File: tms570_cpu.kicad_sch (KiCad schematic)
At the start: 51 parts, among them J12 TS-103-G-A, J2 FTSH-105-01-L-DV-K, U2 TMS570LS0914PGE

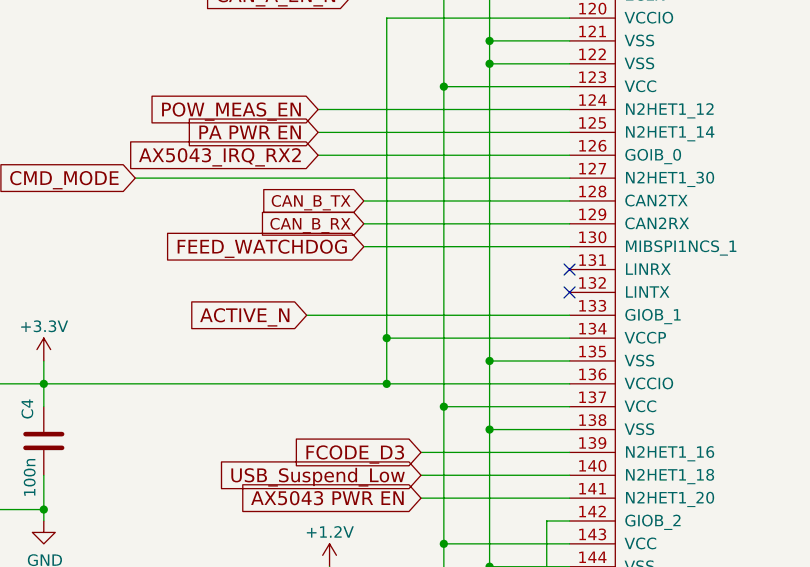
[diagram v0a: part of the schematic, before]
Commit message: Make a little more space around the MRAM
Change the orientation of some resistors.

Signed-off-by: Corey Minyard <corey@minyard.net>
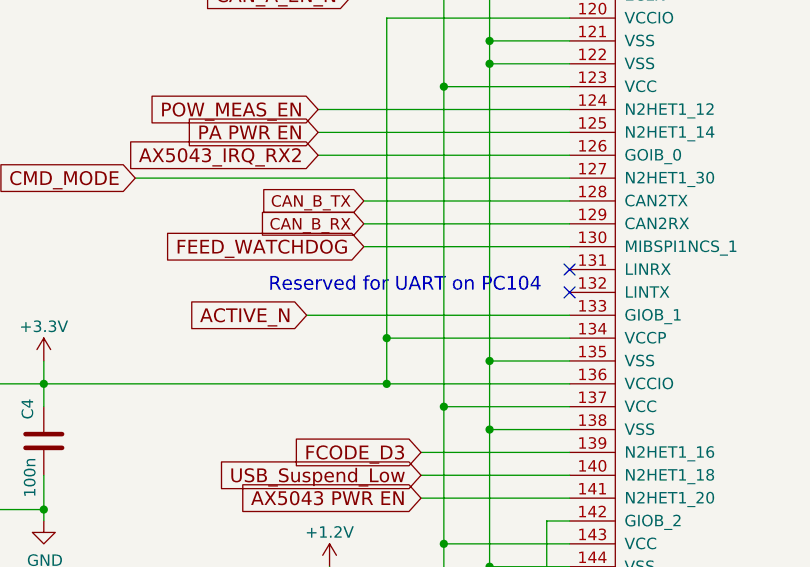
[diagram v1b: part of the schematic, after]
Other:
- note added: "Reserved for UART on PC104"
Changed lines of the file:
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@@
+		)
+	)
+	(text "Reserved for UART on PC104"
+		(exclude_from_sim no)
+		(at 131.572 154.178 0)
+		(effects
+			(font
+				(size 1.524 1.524)
+			)
 		)
 	)

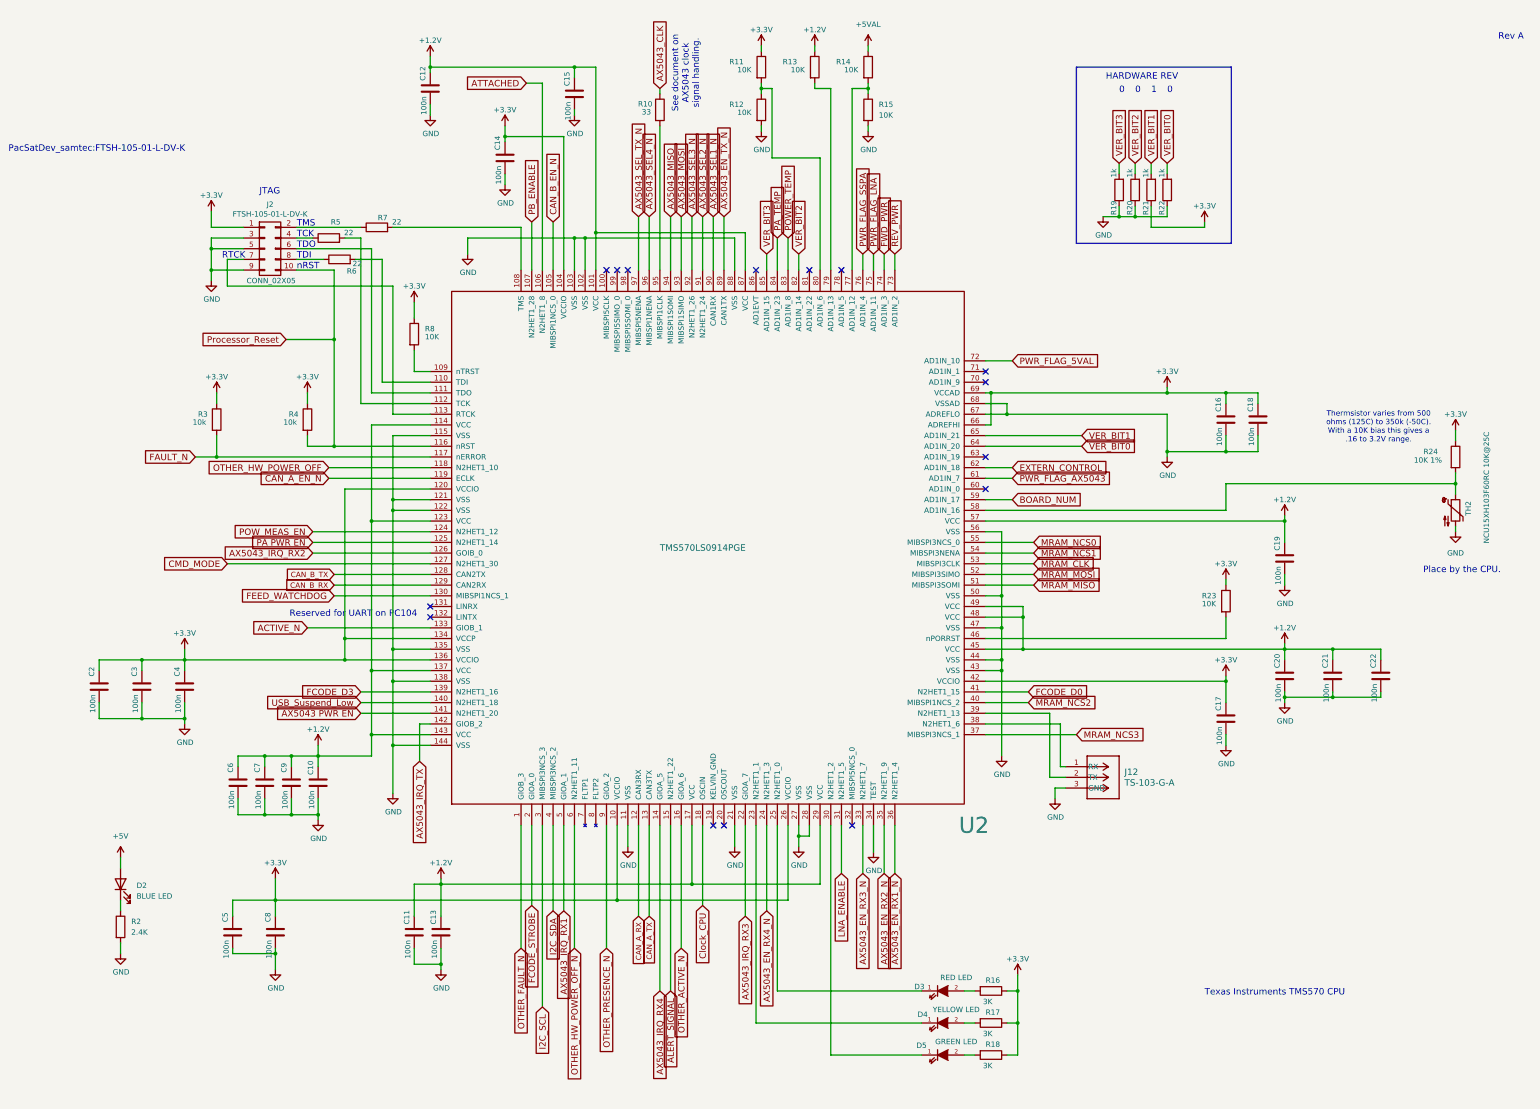
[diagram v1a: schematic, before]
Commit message: Lots of updates to ease manufacturing
Component changes, changes in the formatting of the values, etc.

Signed-off-by: Corey Minyard <corey@minyard.net>
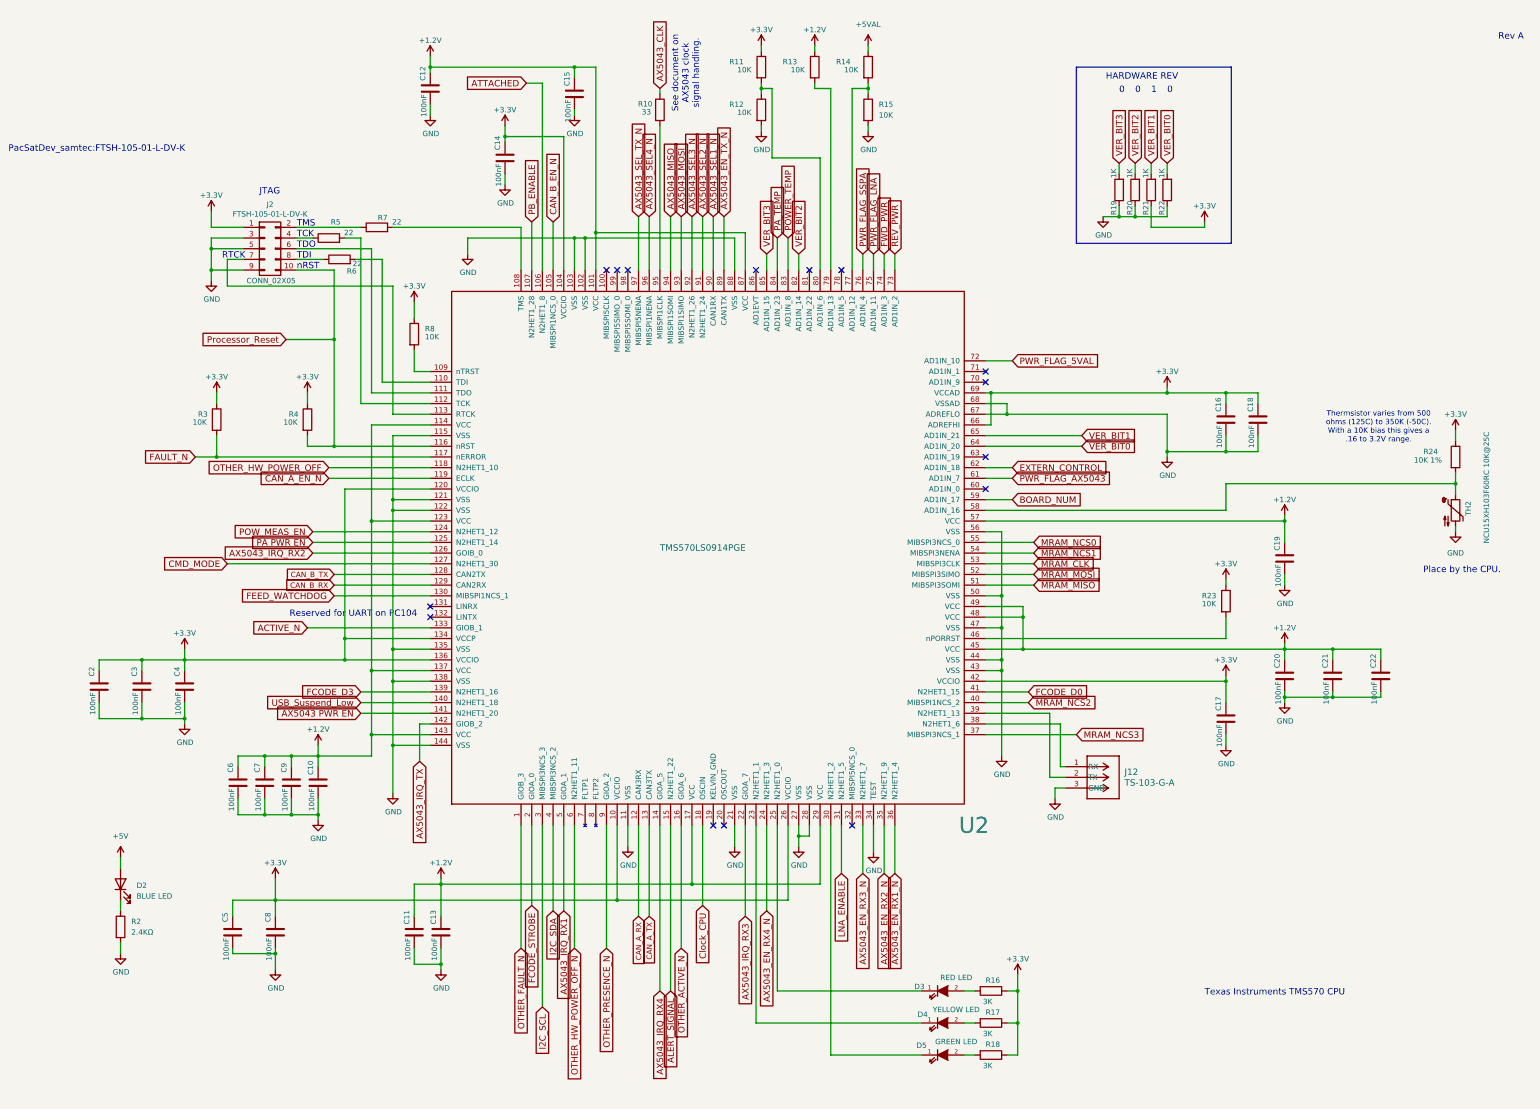
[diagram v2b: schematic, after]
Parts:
- C10, C11, C12, C13, C14, C15, C16, C17, C18, C19, C2, C20, C21, C22, C3, C4, C5, C6, C7, C8, C9: value 100n -> 100nF
- R19, R20, R21, R22: value 1k -> 1K
- R2: value 2.4K -> 2.4KΩ
- R3, R4: value 10k -> 10K
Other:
- note added: "Thermsistor varies from 500 ohms (125C) to 350K (-50C). With a 10K bias this gives a .16 to 3.2V range."
- note removed: "Thermsistor varies from 500 ohms (125C) to 350k (-50C). With a 10K bias this gives a .16 to 3.2V range."
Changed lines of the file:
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@@
 		)
 	)
-	(text "Thermsistor varies from 500\nohms (125C) to 350k (-50C).\nWith a 10K bias this gives a\n.16 to 3.2V range."
+	(text "Thermsistor varies from 500\nohms (125C) to 350K (-50C).\nWith a 10K bias this gives a\n.16 to 3.2V range."
 		(exclude_from_sim no)
 		(at 375.412 109.728 0)
@@
 			)
 		)
-		(property "Value" "10k"
+		(property "Value" "10K"
 			(at 114.935 108.585 0)
 			(effects
@@
 			)
 		)
-		(property "Value" "10k"
+		(property "Value" "10K"
 			(at 93.345 108.585 0)
 			(effects
@@
 			)
 		)
-		(property "Value" "1k"
+		(property "Value" "1K"
 			(at 312.42 48.26 90)
 			(effects
@@
 			)
 		)
-		(property "Value" "1k"
+		(property "Value" "1K"
 			(at 316.23 48.26 90)
 			(effects
@@
 			)
 		)
-		(property "Value" "1k"
+		(property "Value" "1K"
 			(at 320.04 48.26 90)
 			(effects
@@
 			)
 		)
-		(property "Value" "1k"
+		(property "Value" "1K"
 			(at 323.85 48.26 90)
 			(effects
@@
 			)
 		)
-		(property "Value" "100n"
+		(property "Value" "100nF"
 			(at 111.506 233.934 90)
 			(effects
@@
 			)
 		)
-		(property "Value" "100n"
+		(property "Value" "100nF"
 			(at 121.666 198.374 90)
 			(effects
@@
 			)
 		)
-		(property "Value" "100n"
+		(property "Value" "100nF"
 			(at 351.536 145.034 90)
 			(effects
@@
 			)
 		)
-		(property "Value" "100n"
+		(property "Value" "100nF"
 			(at 150.876 233.934 90)
 			(effects
@@
 			)
 		)
-		(property "Value" "100n"
+		(property "Value" "100nF"
 			(at 108.966 198.374 90)
 			(effects
@@
 			)
 		)
-		(property "Value" "100n"
+		(property "Value" "100nF"
 			(at 345.186 112.014 90)
 			(effects
@@
 			)
 		)
-		(property "Value" "100n"
+		(property "Value" "100nF"
 			(at 351.536 172.974 90)
 			(effects
@@
 			)
 		)
-		(property "Value" "100n"
+		(property "Value" "100nF"
 			(at 79.756 175.514 90)
 			(effects
@@
 			)
 		)
-		(property "Value" "100n"
+		(property "Value" "100nF"
 			(at 101.346 233.934 90)
 			(effects
@@
 			)
 		)
-		(property "Value" "100n"
+		(property "Value" "100nF"
 			(at 115.316 198.374 90)
 			(effects
@@
 		(fields_autoplaced yes)
 		(property "Reference" "R2"
-			(at 78.74 227.33 0)
+			(at 78.74 227.3299 0)
 			(effects
 				(font
@@
 			)
 		)
-		(property "Value" "2.4K"
-			(at 78.74 229.87 0)
+		(property "Value" "2.4KΩ"
+			(at 78.74 229.8699 0)
 			(effects
 				(font
@@
 			)
 		)
-		(property "Value" "100n"
+		(property "Value" "100nF"
 			(at 166.116 49.784 90)
 			(effects
@@
 			)
 		)
-		(property "Value" "100n"
+		(property "Value" "100nF"
 			(at 148.336 33.274 90)
 			(effects
@@
 			)
 		)
-		(property "Value" "100n"
+		(property "Value" "100nF"
 			(at 362.966 172.974 90)
 			(effects
@@
 			)
 		)
-		(property "Value" "100n"
+		(property "Value" "100nF"
 			(at 182.626 34.544 90)
 			(effects
@@
 			)
 		)
-		(property "Value" "100n"
+		(property "Value" "100nF"
 			(at 89.916 175.514 90)
 			(effects
@@
 			)
 		)
-		(property "Value" "100n"
+		(property "Value" "100nF"
 			(at 337.566 112.014 90)
 			(effects
@@
 			)
 		)
-		(property "Value" "100n"
+		(property "Value" "100nF"
 			(at 144.526 233.934 90)
 			(effects
@@
 			)
 		)
-		(property "Value" "100n"
+		(property "Value" "100nF"
 			(at 69.596 175.514 90)
 			(effects
@@
 			)
 		)
-		(property "Value" "100n"
+		(property "Value" "100nF"
 			(at 374.396 172.974 90)
 			(effects
@@
 			)
 		)
-		(property "Value" "100n"
+		(property "Value" "100nF"
 			(at 337.566 183.134 90)
 			(effects
@@
 			)
 		)
-		(property "Value" "100n"
+		(property "Value" "100nF"
 			(at 102.616 198.374 90)
 			(effects

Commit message: Update all resistors to have an ohm symbol
Make it more clean in the BOM what they are.

Signed-off-by: Corey Minyard <corey@minyard.net>
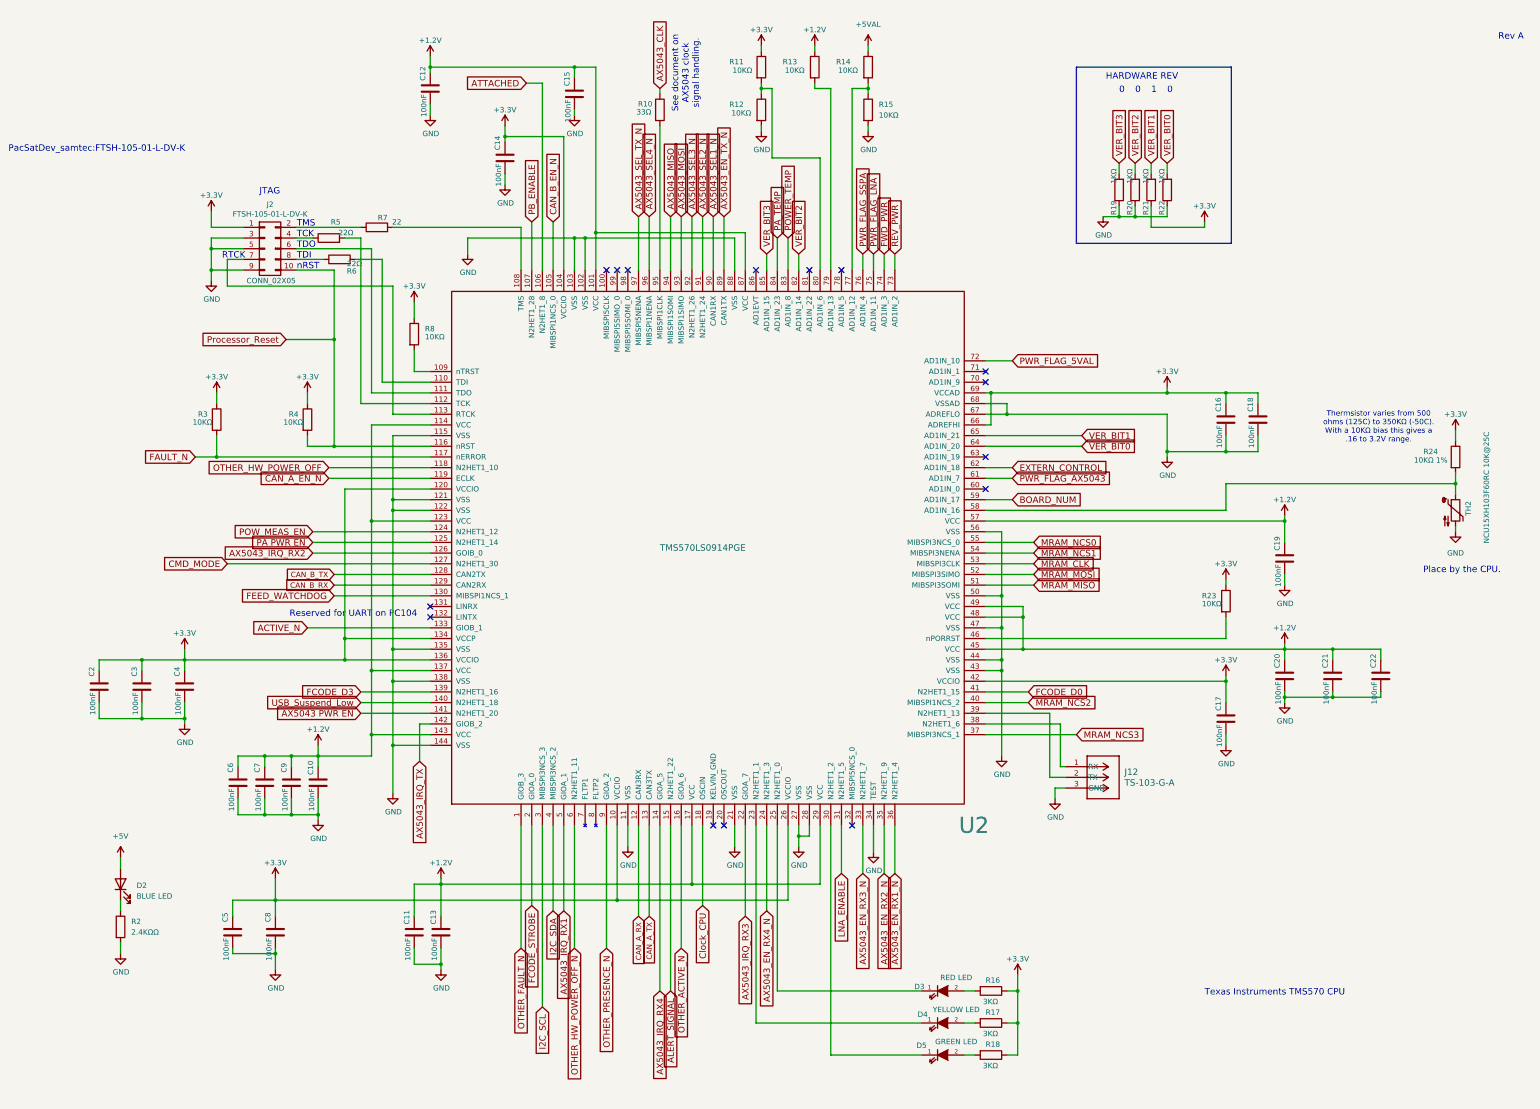
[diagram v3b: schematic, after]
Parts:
- R10: value 33 -> 33Ω
- R11, R12, R13, R14, R15, R23, R3, R4, R8: value 10K -> 10KΩ
- R16, R17, R18: value 3K -> 3KΩ
- R19, R20, R21, R22: value 1K -> 1KΩ
- R2: value 2.4KΩ -> 2.4KΩΩ
- R24: value 10K 1% -> 10KΩ 1%
- R5, R6: value 22 -> 22Ω
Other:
- note added: "Thermsistor varies from 500 ohms (125C) to 350KΩ (-50C). With a 10KΩ bias this gives a .16 to 3.2V range."
- note removed: "Thermsistor varies from 500 ohms (125C) to 350K (-50C). With a 10K bias this gives a .16 to 3.2V range."
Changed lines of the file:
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@@
 		)
 	)
-	(text "Thermsistor varies from 500\nohms (125C) to 350K (-50C).\nWith a 10K bias this gives a\n.16 to 3.2V range."
+	(text "Thermsistor varies from 500\nohms (125C) to 350KΩ (-50C).\nWith a 10KΩ bias this gives a\n.16 to 3.2V range."
 		(exclude_from_sim no)
 		(at 375.412 109.728 0)
@@
 			)
 		)
-		(property "Value" "10K"
+		(property "Value" "10KΩ"
 			(at 114.935 108.585 0)
 			(effects
@@
 			)
 		)
-		(property "Value" "10K"
+		(property "Value" "10KΩ"
 			(at 148.59 88.265 0)
 			(effects
@@
 			)
 		)
-		(property "Value" "10K"
+		(property "Value" "10KΩ"
 			(at 93.345 108.585 0)
 			(effects
@@
 			)
 		)
-		(property "Value" "3K"
+		(property "Value" "3KΩ"
 			(at 281.305 246.38 90)
 			(effects
@@
 			)
 		)
-		(property "Value" "3K"
+		(property "Value" "3KΩ"
 			(at 281.305 254 90)
 			(effects
@@
 			)
 		)
-		(property "Value" "3K"
+		(property "Value" "3KΩ"
 			(at 281.305 261.62 90)
 			(effects
@@
 			)
 		)
-		(property "Value" "10K"
+		(property "Value" "10KΩ"
 			(at 333.375 151.765 0)
 			(effects
@@
 			)
 		)
-		(property "Value" "1K"
+		(property "Value" "1KΩ"
 			(at 312.42 48.26 90)
 			(effects
@@
 			)
 		)
-		(property "Value" "1K"
+		(property "Value" "1KΩ"
 			(at 316.23 48.26 90)
 			(effects
@@
 			)
 		)
-		(property "Value" "1K"
+		(property "Value" "1KΩ"
 			(at 320.04 48.26 90)
 			(effects
@@
 			)
 		)
-		(property "Value" "1K"
+		(property "Value" "1KΩ"
 			(at 323.85 48.26 90)
 			(effects
@@
 			)
 		)
-		(property "Value" "10K"
-			(at 235.585 24.765 0)
+		(property "Value" "10KΩ"
+			(at 234.188 24.892 0)
 			(effects
 				(font
@@
 			)
 		)
-		(property "Value" "10K"
-			(at 248.285 24.765 0)
+		(property "Value" "10KΩ"
+			(at 246.888 24.892 0)
 			(effects
 				(font
@@
 			)
 		)
-		(property "Value" "10K"
+		(property "Value" "10KΩ"
 			(at 256.54 35.56 0)
 			(effects
@@
 			)
 		)
-		(property "Value" "10K 1%"
+		(property "Value" "10KΩ 1%"
 			(at 383.794 117.602 0)
 			(effects
@@
 			)
 		)
-		(property "Value" "10K"
-			(at 222.885 34.925 0)
+		(property "Value" "10KΩ"
+			(at 221.488 35.052 0)
 			(effects
 				(font
@@
 			)
 		)
-		(property "Value" "22"
+		(property "Value" "22Ω"
 			(at 131.572 63.5 90)
 			(effects
@@
 			)
 		)
-		(property "Value" "2.4KΩ"
+		(property "Value" "2.4KΩΩ"
 			(at 78.74 229.8699 0)
 			(effects
@@
 			)
 		)
-		(property "Value" "10K"
-			(at 222.885 24.765 0)
+		(property "Value" "10KΩ"
+			(at 221.742 24.892 0)
 			(effects
 				(font
@@
 			)
 		)
-		(property "Value" "22"
+		(property "Value" "22Ω"
 			(at 133.604 70.866 90)
 			(effects
@@
 			)
 		)
-		(property "Value" "33"
-			(at 200.152 34.798 0)
+		(property "Value" "33Ω"
+			(at 198.882 34.798 0)
 			(effects
 				(font

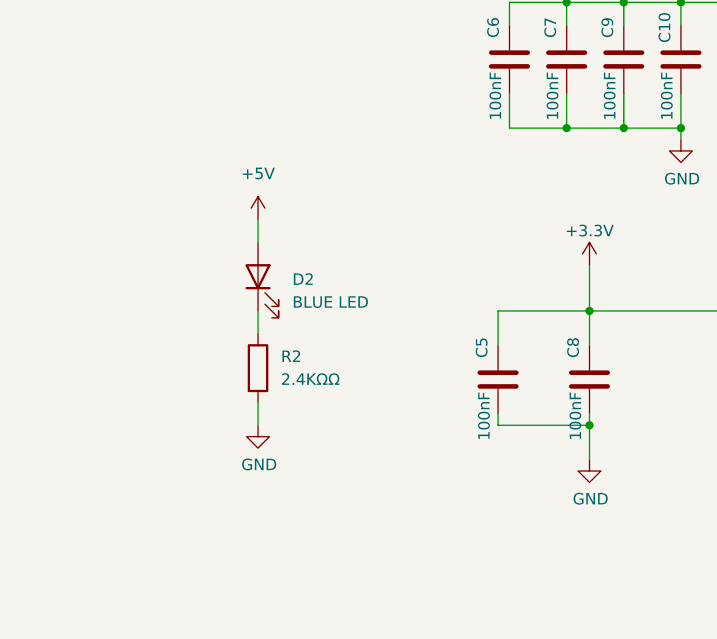
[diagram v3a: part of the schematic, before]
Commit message: More work converting to the CubeSat Kit Bus
Signed-off-by: Corey Minyard <corey@minyard.net>
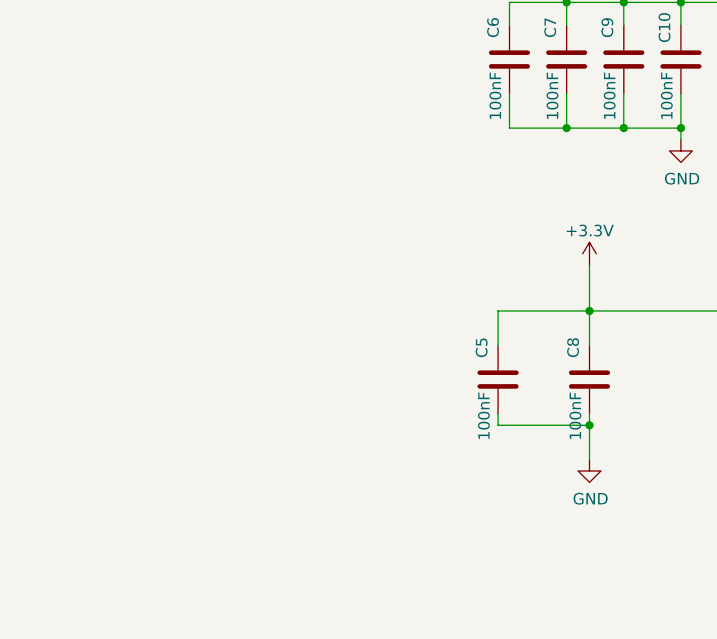
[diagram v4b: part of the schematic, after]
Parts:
- removed D2: BLUE LED, LED_SMD:LED_0603_1608Metric_Pad1.05x0.95mm_HandSolder, symbol Device:LED
- removed R2: 2.4KΩΩ, Resistor_SMD:R_0603_1608Metric_Pad0.98x0.95mm_HandSolder, symbol Device:R
